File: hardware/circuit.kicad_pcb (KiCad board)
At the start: 4 copper layers, 59.5 x 53.2 mm, 64 parts, among them J1 VBUS input fly-leads, J2 Orange TinySLED, J3 Orange TinySLED, J4 AM32 dual ESC, Q1 AO3402, U1 Seeed XIAO RP2350, U10 SK9822-EC20, U11 SN74HC595PWR, U12 SK9822-EC20, U2 AP63205WU-7, U4 LSM6DSV320XTR, U5 H3LIS331DLTR, U6 H3LIS331DLTR, U8 SN74AHCT1G125, U9 SN74AHCT1G125

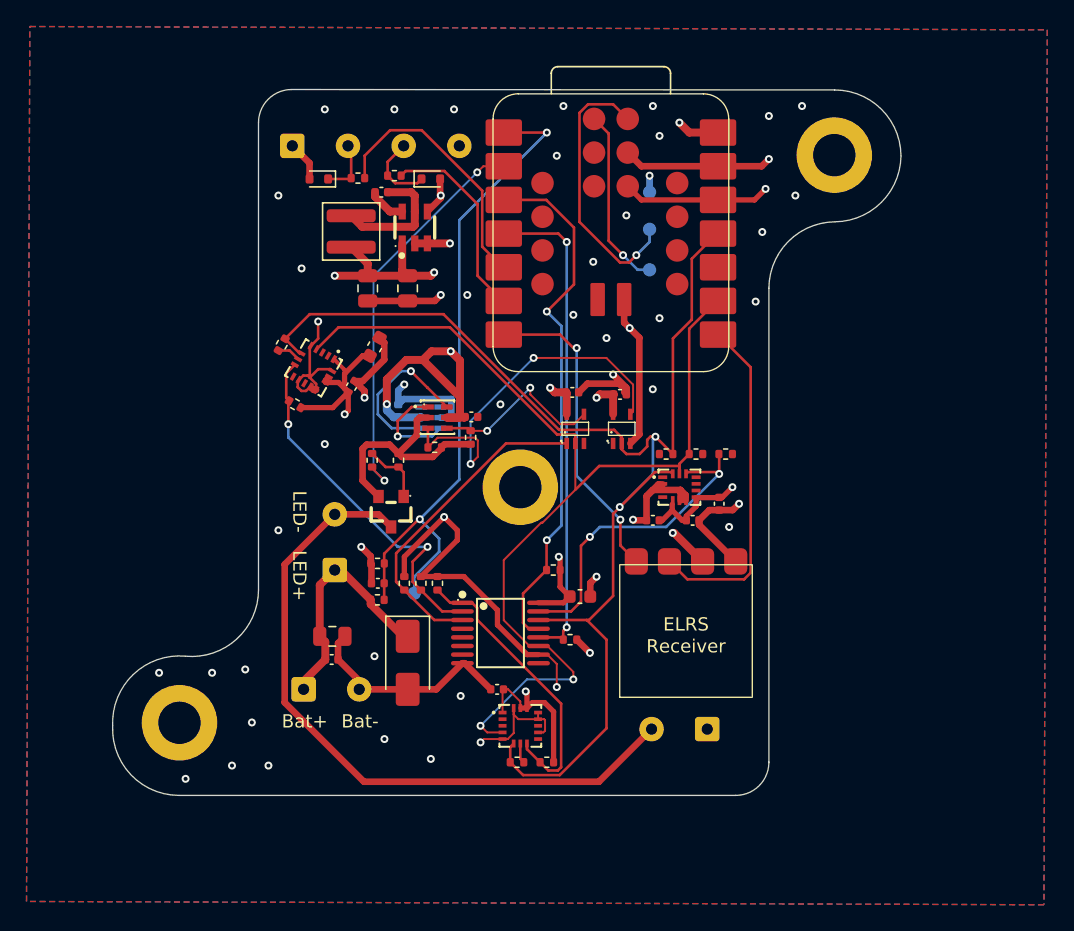
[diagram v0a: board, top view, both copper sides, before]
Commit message: feat: add bom placement
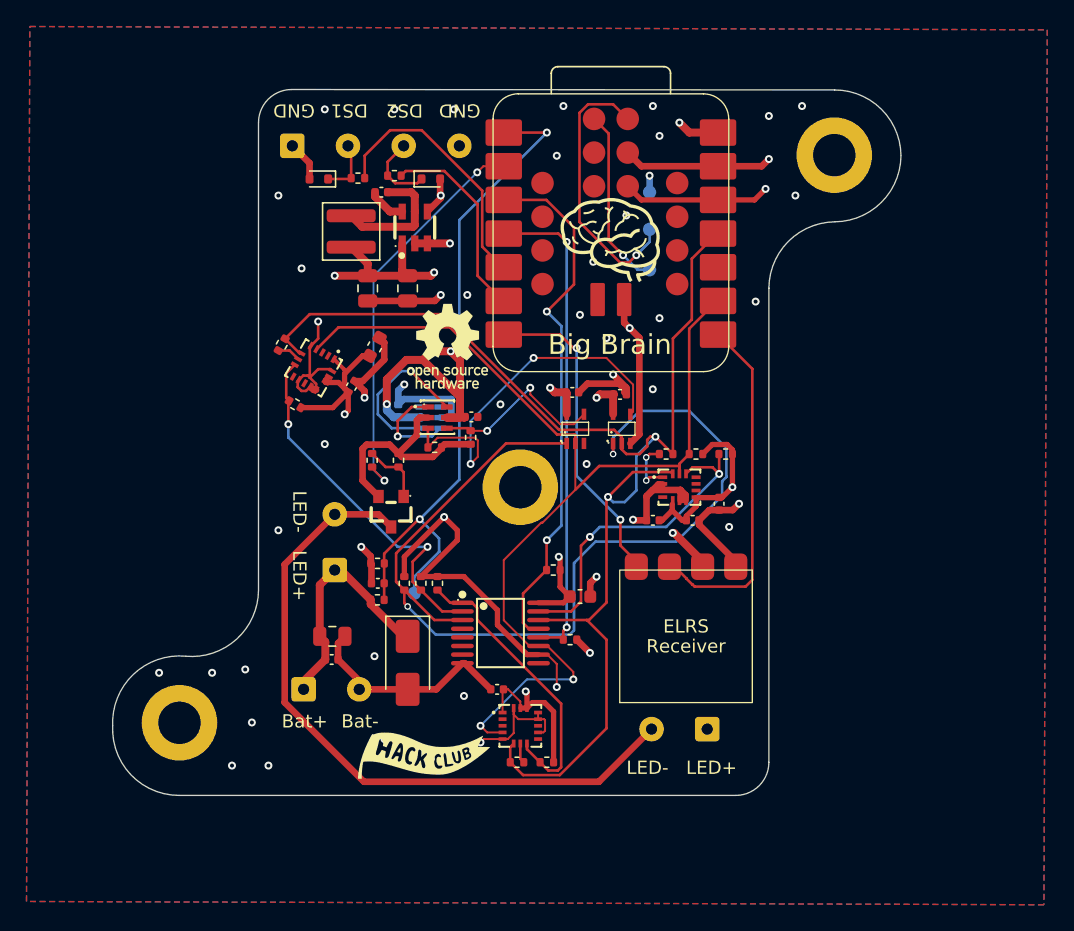
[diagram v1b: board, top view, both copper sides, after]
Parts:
- removed ELRS: BetaFPV ELRS Lite, Library:BetaFPV_ELRS_Lite
- added G***: LOGO, LOGO, F.Cu at (110.5, 84.5)
- added G***: LOGO, LOGO, F.Cu at (96.5, 123.5)
- added U7: BetaFPV ELRS Lite, Library:BetaFPV_ELRS_Lite, F.Cu at (118.0, 115.2)
- R10: value 33kΩ -> 33.2kΩ
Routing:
- net /LED_OE_N: track 24.6 -> 74.2 mm, vias 0 -> 2
- net 3V3: track 78.0 -> 83.5 mm, vias 8 -> 7
- net /IMU Array/MISO_A: track 0.00 -> 4.19 mm, vias 0 -> 2
- net /SPI_MOSI: track 100.4 -> 102.2 mm
- net /CRSF_RX: track 25.9 -> 26.8 mm
- net VBUS: vias 2 -> 1
- net GND: vias 49 -> 50
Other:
- board text added: "Big Brain"
- board text added: "DS1"
- board text added: "DS2"
- board text added: "ELRS"
- board text added: "GND"

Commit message: feat: add pulldown resister and note mode 0
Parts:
- added R22: 100kΩ, Resistor_SMD:R_0402_1005Metric, F.Cu at (117.0, 99.0)
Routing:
- net GND: track 133.4 -> 135.0 mm, vias 50 -> 51
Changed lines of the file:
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@@
 		)
 	)
+	(footprint "Resistor_SMD:R_0402_1005Metric"
+		(layer "F.Cu")
+		(at 116.955 99)
+		(descr "Resistor SMD 0402 (1005 Metric), square (rectangular) end terminal, IPC-7351 nominal, (Body size source: IPC-SM-782 page 72, https://www.pcb-3d.com/wordpress/wp-content/uploads/ipc-sm-782a_amendment_1_and_2.pdf)")
+		(tags "resistor")
+		(property "Reference" "R22"
+			(at 0 -1.17 0)
+			(layer "F.SilkS")
+			(effects
+				(font
+					(size 1 1)
+					(thickness 0.15)
+				)
+			)
+		)
+		(property "Value" "100kΩ"
+			(at 0 1.17 0)
+			(layer "F.Fab")
+			(effects
+				(font
+					(size 1 1)
+					(thickness 0.15)
+				)
+			)
+		)
+		(property "Datasheet" "~"
+			(at 0 0 0)
+			(layer "F.Fab")
+			(hide yes)
+			(effects
+				(font
+					(size 1.27 1.27)
+				)
+			)
+		)
+		(property "Description" ""
+			(at 0 0 0)
+			(layer "F.Fab")
+			(hide yes)
+			(effects
+				(font
+					(size 1.27 1.27)
+				)
+			)
+		)
+		(property "KiLib_Generator" "SMD_2terminal_chip_molded"
+			(at 0 0 0)
+			(layer "F.SilkS")
+			(hide yes)
+			(effects
+				(font
+					(size 1 1)
+					(thickness 0.15)
+				)
+			)
+		)
+		(property "LCSC Part" "C2077080"
+			(at 0 0 0)
+			(unlocked yes)
+			(layer "F.Fab")
+			(hide yes)
+			(effects
+				(font
+					(size 1 1)
+					(thickness 0.15)
+				)
+			)
+		)
+		(property ki_fp_filters "R_*")
+		(sheetname "/IMU Array/")
+		(sheetfile "schm/imu_array.kicad_sch")
+		(units
+			(unit
+				(name "A")
+				(pins "1" "2")
+			)
+		)
+		(attr smd)
+		(duplicate_pad_numbers_are_jumpers no)
+		(fp_line
+			(start -0.153641 -0.38)
+			(end 0.153641 -0.38)
+			(stroke
+				(width 0.12)
+				(type solid)
+			)
+			(layer "F.SilkS")
+		)
+		(fp_line
+			(start -0.153641 0.38)
+			(end 0.153641 0.38)
+			(stroke
+				(width 0.12)
+				(type solid)
+			)
+			(layer "F.SilkS")
+		)
+		(fp_rect
+			(start -0.93 -0.47)
+			(end 0.93 0.47)
+			(stroke
+				(width 0.05)
+				(type solid)
+			)
+			(fill no)
+			(layer "F.CrtYd")
+		)
+		(fp_rect
+			(start -0.525 -0.27)
+			(end 0.525 0.27)
+			(stroke
+				(width 0.1)
+				(type solid)
+			)
+			(fill no)
+			(layer "F.Fab")
+		)
+		(fp_text user "${REFERENCE}"
+			(at 0 0 0)
+			(layer "F.Fab")
+			(effects
+				(font
+					(size 0.26 0.26)
+					(thickness 0.04)
+				)
+			)
+		)
+		(pad "1" smd roundrect
+			(at -0.51 0)
+			(size 0.54 0.64)
+			(layers "F.Cu" "F.Mask" "F.Paste")
+			(roundrect_rratio 0.25)
+			(net "/SPI_SCK")
+			(pintype "passive")
+		)
+		(pad "2" smd roundrect
+			(at 0.51 0)
+			(size 0.54 0.64)
+			(layers "F.Cu" "F.Mask" "F.Paste")
+			(roundrect_rratio 0.25)
+			(net "GND")
+			(pintype "passive")
+		)
+		(embedded_fonts no)
+		(model "${KICAD10_3DMODEL_DIR}/Resistor_SMD.3dshapes/R_0402_1005Metric.step"
+			(offset
+				(xyz 0 0 0)
+			)
+			(scale
+				(xyz 1 1 1)
+			)
+			(rotate
+				(xyz 0 0 0)
+			)
+		)
+	)
 	(footprint "Library:LED-SMD_6P-L2.0-W2.0-P0.80-TL"
 		(placed yes)
@@
 	)
 	(segment
+		(start 118 99)
+		(end 118.75 98.25)
+		(width 0.5)
+		(layer "F.Cu")
+		(net "GND")
+	)
+	(segment
 		(start 87.583205 95.990282)
 		(end 87.913013 95.660474)
@@
 	)
 	(segment
+		(start 117.465 99)
+		(end 118 99)
+		(width 0.5)
+		(layer "F.Cu")
+		(net "GND")
+	)
+	(segment
 		(start 88.5 92.043501)
 		(end 88.5 90.75)
@@
 	)
 	(via
+		(at 118.75 98.25)
+		(size 0.6)
+		(drill 0.3)
+		(layers "F.Cu" "B.Cu")
+		(net "GND")
+	)
+	(via
 		(at 100.75 122.5)
 		(size 0.6)
@@
 			"27e27698-39cf-4635-bf9d-c79d9dbe905a" "334fcc8b-d5af-42d0-ae13-cc0f5a8ec1bf"
 			"351820e8-cb6c-4b2b-8679-93cf9908d2cd" "404c9d0f-e62c-43bd-918a-2c51441bfc93"
-			"42517178-9ec6-4db4-a1c9-e821f3cef5d9" "4b55ffc5-23da-4e2b-ac5a-9a2f230d887e"
-			"4e9d5720-49f8-4206-bdb6-33af0647420e" "52392ba1-9360-4f84-8ee3-55ebcb4a4754"
-			"536e9e03-1389-4c75-aa64-78e95c866054" "545f3603-a310-4765-a2d1-3ccc2a373099"
-			"5a5eece3-124d-475f-9ced-6ac58a0cf103" "5bef76ba-cdb1-4509-8af1-c6c1af4b92b1"
-			"8a655a1a-2134-4fd0-b2a1-4f39ddfba055" "9d3de96a-8921-4b9f-bccb-ff52220f3c7b"
-			"a23a6439-a305-4470-943a-79726b47073b" "b9c72bb1-58b1-4dcd-9089-24d3cb4750f1"
-			"b9da47c2-6cf8-426f-8a5b-41d7db9abdf8"
+			"42517178-9ec6-4db4-a1c9-e821f3cef5d9" "4e9d5720-49f8-4206-bdb6-33af0647420e"
+			"52392ba1-9360-4f84-8ee3-55ebcb4a4754" "536e9e03-1389-4c75-aa64-78e95c866054"
+			"545f3603-a310-4765-a2d1-3ccc2a373099" "5a5eece3-124d-475f-9ced-6ac58a0cf103"
+			"5bef76ba-cdb1-4509-8af1-c6c1af4b92b1" "8a655a1a-2134-4fd0-b2a1-4f39ddfba055"
+			"9d3de96a-8921-4b9f-bccb-ff52220f3c7b" "a23a6439-a305-4470-943a-79726b47073b"
+			"b9c72bb1-58b1-4dcd-9089-24d3cb4750f1" "b9da47c2-6cf8-426f-8a5b-41d7db9abdf8"
 		)
 	)

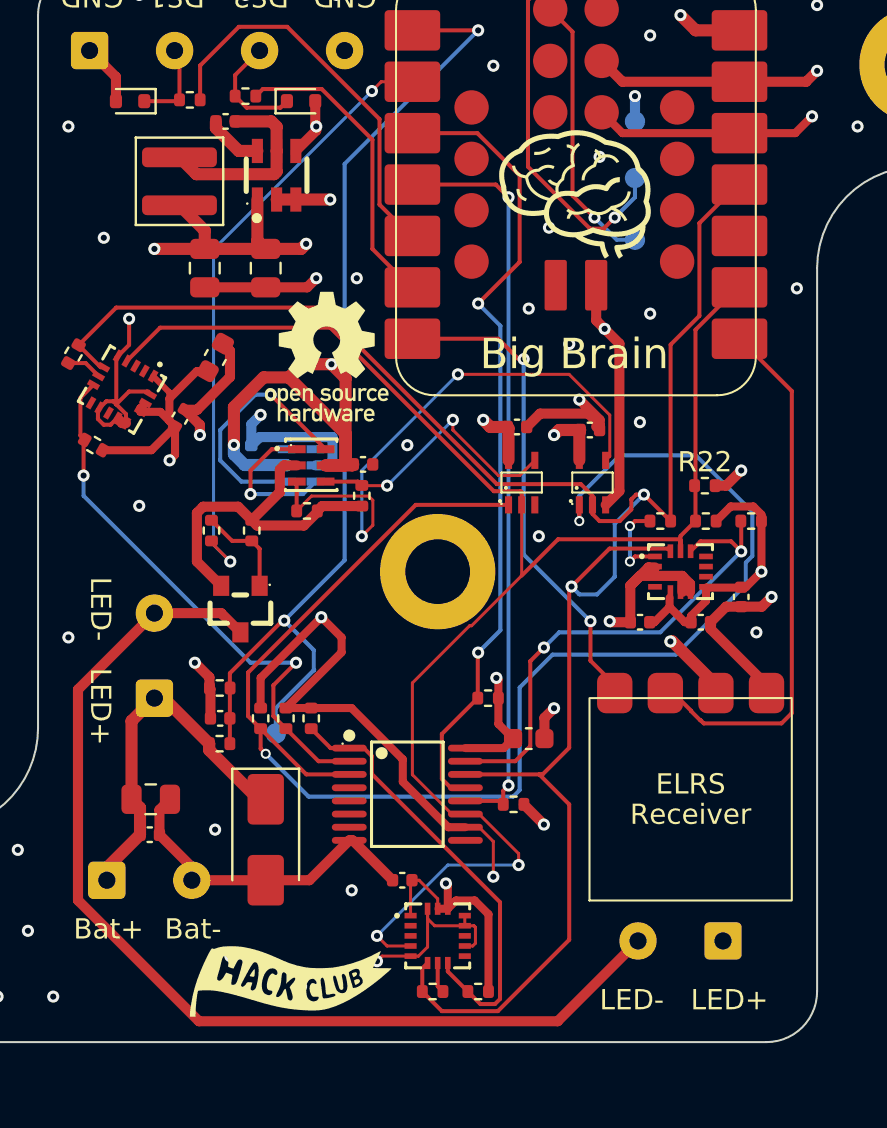
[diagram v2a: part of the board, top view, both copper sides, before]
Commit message: feat: review from tyler + align circuit.py
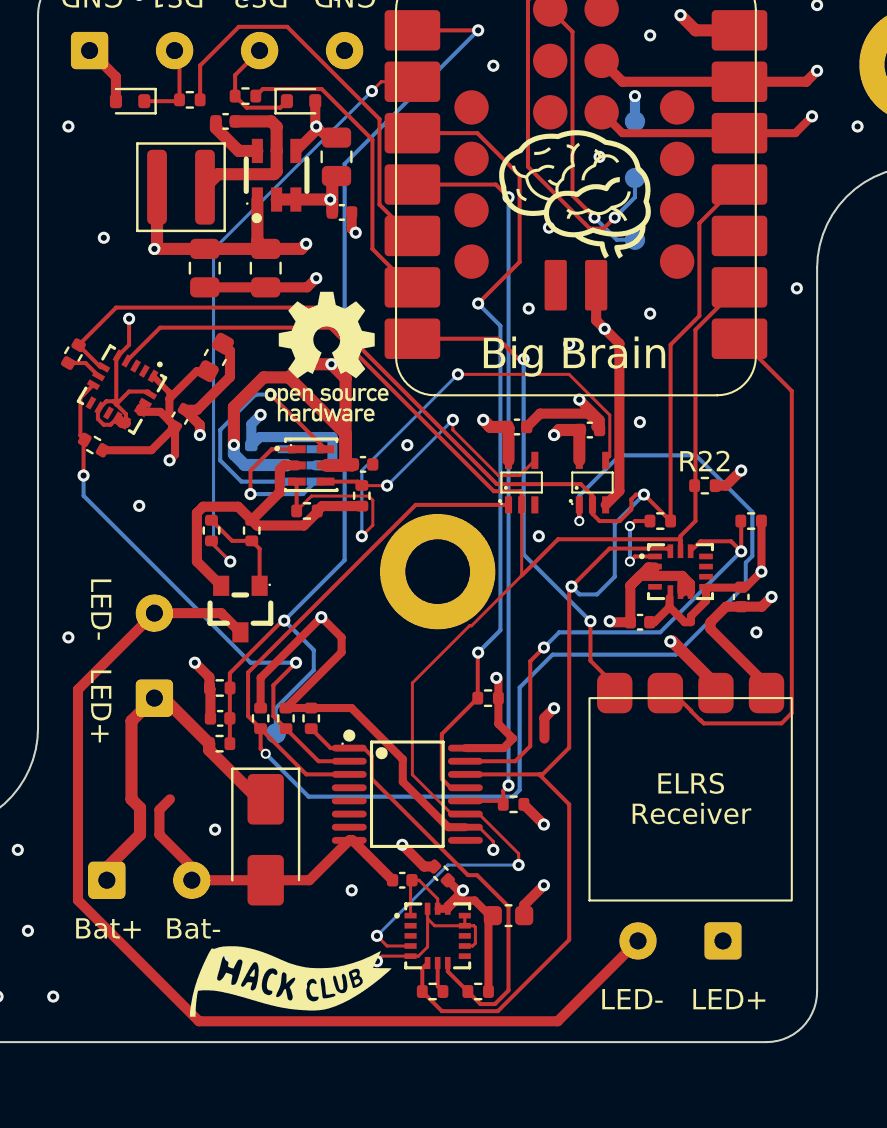
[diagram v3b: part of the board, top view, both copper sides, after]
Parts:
- removed R3: 10kΩ, Resistor_SMD:R_0402_1005Metric
- moved C1 33.1 mm to (98.8, 82.8), turned to 90 degrees
- moved C2 32.2 mm to (99.0, 85.5)
- moved C9 17.9 mm to (103.9, 118.2), turned to 135 degrees
- moved C13 8.81 mm to (107.2, 120.2)
- moved L1 0.30 mm to (91.1, 84.2), turned to 180 degrees
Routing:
- net GND: track 135.0 -> 141.2 mm, vias 51 -> 53
- net 3V3: track 83.5 -> 80.1 mm
- net VBUS: track 60.6 -> 62.6 mm
- net Net-(U2-SW): track 9.57 -> 8.23 mm
- net /IMU Array/CS_B: track 22.4 -> 23.0 mm

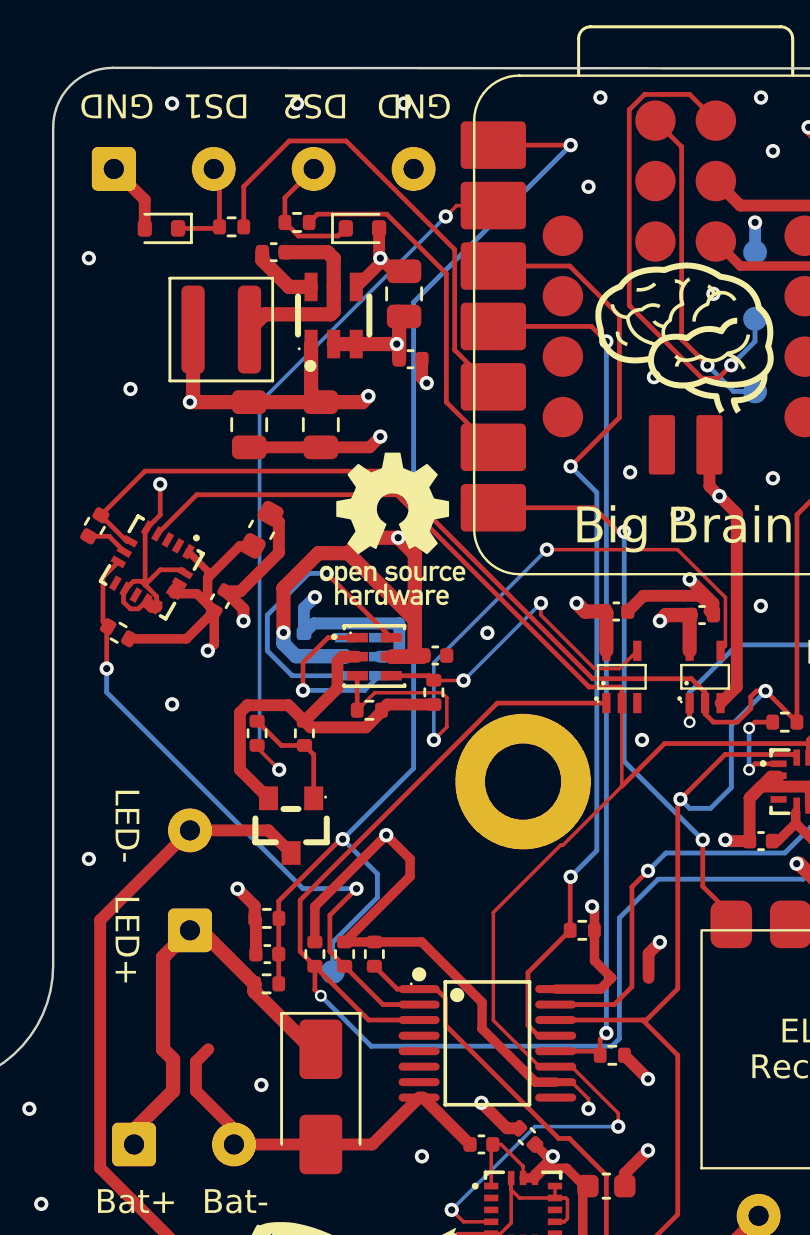
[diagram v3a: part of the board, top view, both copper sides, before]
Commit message: feat: add jumper for shutoff voltage
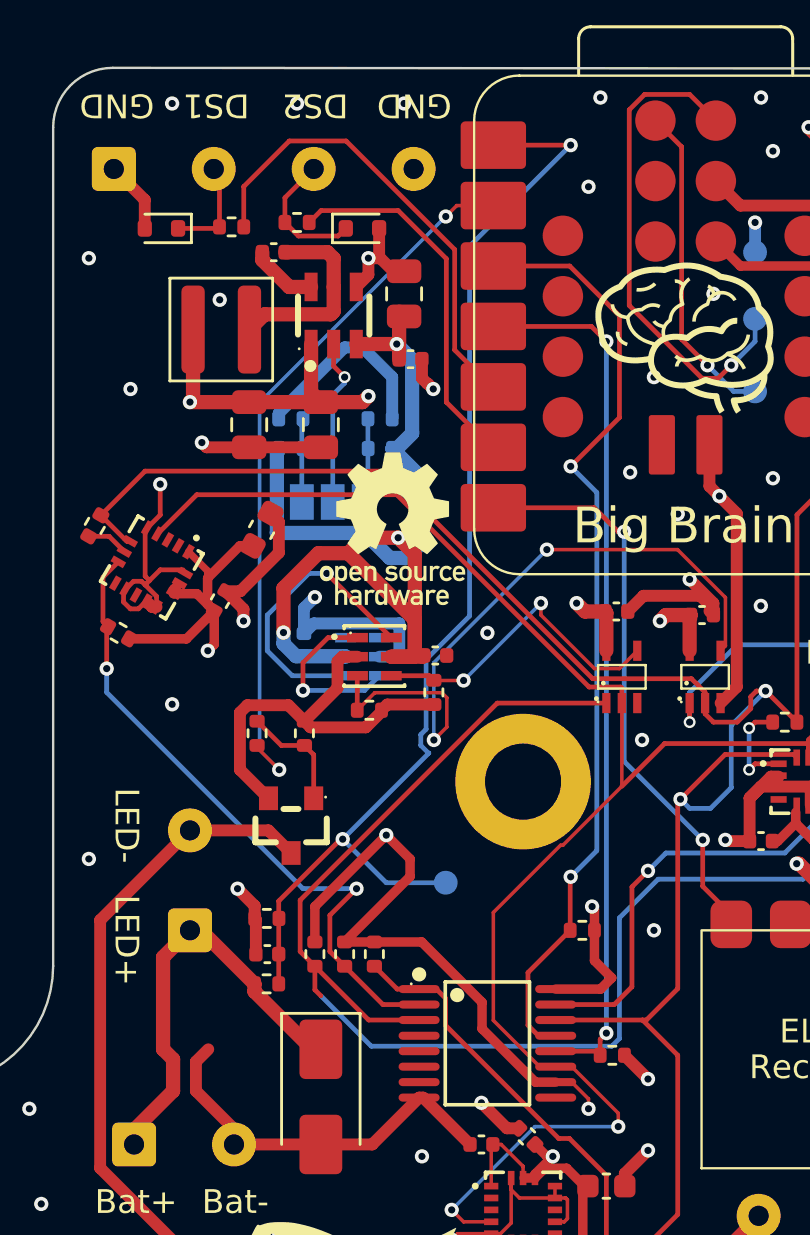
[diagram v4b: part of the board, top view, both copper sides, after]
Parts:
- added JP1: UNVLO_SEL, Jumper:SolderJumper-3_P1.3mm_Open_Pad1.0x1.5mm, B.Cu at (95.8, 91.5)
- added R23: 47kΩ, Resistor_SMD:R_0402_1005Metric, B.Cu at (94.0, 89.2)
- added R24: 10kΩ, Resistor_SMD:R_0402_1005Metric, B.Cu at (94.0, 88.0)
- added R25: 75kΩ, Resistor_SMD:R_0402_1005Metric, B.Cu at (97.8, 89.2)
- added R26: 10kΩ, Resistor_SMD:R_0402_1005Metric, B.Cu at (97.7, 88.0)
- moved TP10 6.05 mm to (100.5, 107.5)
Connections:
- U2 pad 2: VBUS -> /Power Subsystem/BUCK_EN
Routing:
- net VBUS: track 62.6 -> 81.5 mm
- net GND: track 141.2 -> 148.3 mm
- net /Power Subsystem/BUCK_EN: track 0.00 -> 7.04 mm, vias 0 -> 1
- net /Power Subsystem/UVLO_3S: track 0.00 -> 3.09 mm
- net /Power Subsystem/UVLO_2S: track 0.00 -> 3.02 mm
- net /VBAT_SNS: track 50.6 -> 49.0 mm
- net /LED_OE_N: vias 2 -> 1
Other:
- board text added: "3S EN 2S"
- board text added: "OPEN = BYPASS"
